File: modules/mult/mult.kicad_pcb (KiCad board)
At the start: 2 copper layers, 18.5 x 111.5 mm, 9 parts, among them J1 Thonkiconn, J2 Thonkiconn, J3 Thonkiconn, J4 Thonkiconn, J5 Thonkiconn, J6 Thonkiconn, J7 Thonkiconn, J8 Thonkiconn

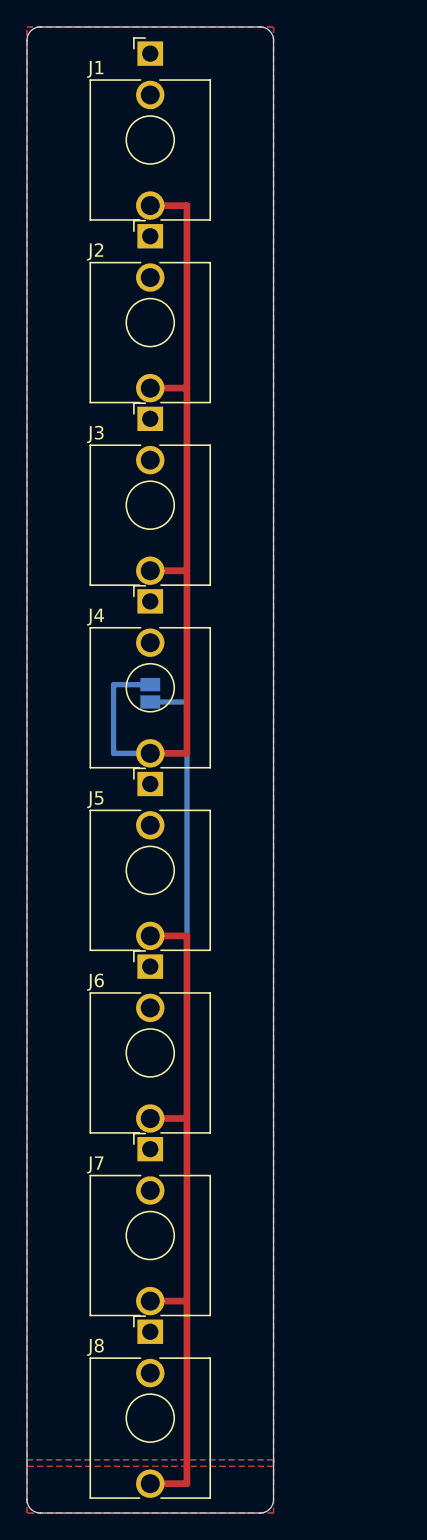
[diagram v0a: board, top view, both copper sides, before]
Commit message: Generate KiCad projects from Haskell: pcbgen toolkit, regenerated mult
toolkit/ is a cabal project that turns a design description
(toolkit/src/Designs/<Name>.hs) into a complete KiCad 10 project: schematic
with embedded library symbols, board with embedded library footprints, project
file with design rules, and custom DRC rules. UUIDs are derived from stable
seeds so regeneration is byte-identical. toolkit/check.sh runs ERC, DRC with
zone refill and schematic parity on a copy in build/, and renders both sides.

modules/mult is now generated. With --severity-all it has zero ERC violations,
zero DRC violations, zero unconnected items and zero parity issues. The
Konnect-made board it replaces had nine library-mismatch warnings and needed
GUI steps to finish.

README.md explains the tool choices (KiCad as compile target, kicad-cli,
KiKit for fab export, Konnect read-only). SETUP.md and CLAUDE.md follow the
new workflow.

Co-Authored-By: Claude Fable 5.1 <noreply@anthropic.com>
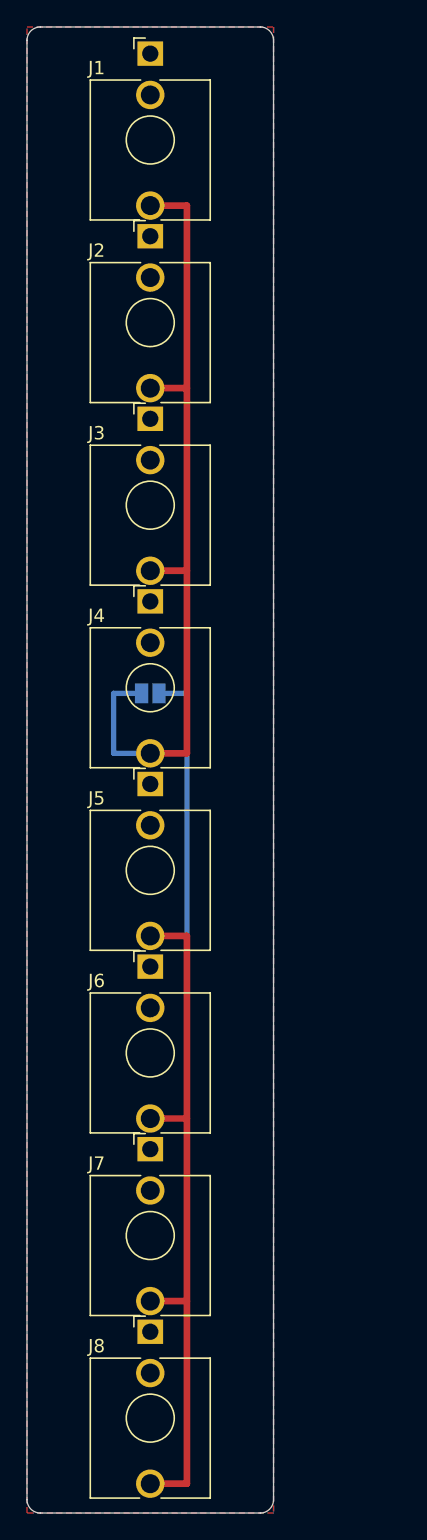
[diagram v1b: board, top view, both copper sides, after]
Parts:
- turned JP1 to 0 degrees
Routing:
- net /MULT_A: track 62.8 -> 61.5 mm
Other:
- board text added: "LINK A-B"
- board text added: "MULT 2x4"

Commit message: Fix Eurorack dimensions: mult becomes 6HP 2x6, add panel project and KiKit export
Doepfer's construction notes and the rail-clearance consensus (PCB <= 108 mm,
centred) showed the 4HP eight-jack column could not fit: the official
Thonkiconn footprint forces a 13.6 mm pitch, and eight of them plus the
barrel and the last body need 110.7 mm. The module is now 6HP with two
columns of six on a 28 x 108 mm board centred behind a 30 x 128.5 mm panel.

- Design.eurorackPanelWidth uses Doepfer's width table; panel height is a
  named constant.
- Designs.MultPanel generates the front panel as its own KiCad project
  (modules/mult/panel) from the same geometry; rail holes at Doepfer
  positions, 6.4 mm jack holes, legend on F.SilkS.
- pcbgen gains 'all' and per-design output directories; parts can hide
  their reference on silkscreen.
- check.sh takes a module sub-directory; fab.sh runs KiKit 1.8.1 (installed
  in KiCad's Python) with --no-drc because its own DRC pass crashes in the
  KiCad 10 bindings. Gerber extents verified: 28.00 x 108.00 and
  30.00 x 128.50 mm.
- Both projects: ERC clean, DRC clean with parity, zero unconnected.

Co-Authored-By: Claude Fable 5.1 <noreply@anthropic.com>
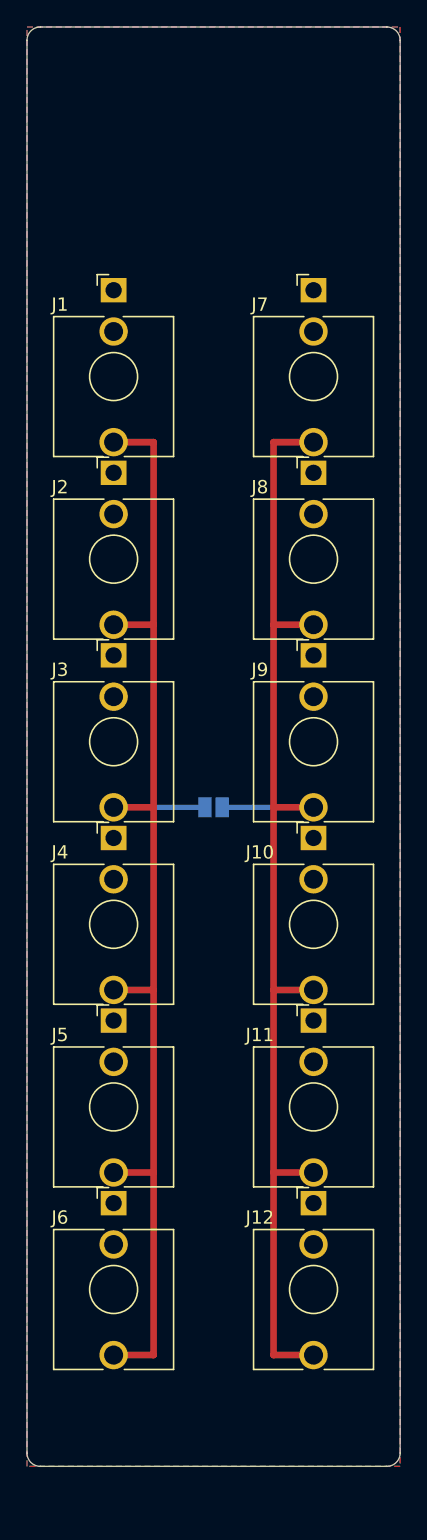
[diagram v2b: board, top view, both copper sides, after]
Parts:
- added J10: Thonkiconn, Connector_Audio:Jack_3.5mm_QingPu_WQP-PJ398SM_Vertical_CircularHoles, F.Cu at (21.5, 60.9)
- added J11: Thonkiconn, Connector_Audio:Jack_3.5mm_QingPu_WQP-PJ398SM_Vertical_CircularHoles, F.Cu at (21.5, 74.5)
- added J12: Thonkiconn, Connector_Audio:Jack_3.5mm_QingPu_WQP-PJ398SM_Vertical_CircularHoles, F.Cu at (21.5, 88.2)
- added J9: Thonkiconn, Connector_Audio:Jack_3.5mm_QingPu_WQP-PJ398SM_Vertical_CircularHoles, F.Cu at (21.5, 47.1)
- moved J7 65.6 mm to (21.5, 19.8)
- moved J8 65.6 mm to (21.5, 33.5)
- moved J2 18.0 mm to (6.50, 33.5)
- moved J1 18.0 mm to (6.50, 19.8)
- moved J3 18.0 mm to (6.50, 47.1)
- moved J4 18.0 mm to (6.50, 60.9)
- moved J5 18.0 mm to (6.50, 74.5)
- moved J6 18.0 mm to (6.50, 88.2)
- moved JP1 9.78 mm to (14.0, 58.5)
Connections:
- J5 pad T: /MULT_B -> /MULT_A
- J6 pad T: /MULT_B -> /MULT_A
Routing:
- net /MULT_A: track 61.5 -> 93.3 mm
- net /MULT_B: track 75.2 -> 93.3 mm
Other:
- board size 18.5 x 111.5 mm -> 28 x 108 mm
- board text added: "A"
- board text added: "B"
- board text added: "MULT 2x6"
- board text removed: "MULT 2x4"

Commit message: Add grid autorouter (A* + negotiated congestion) and route the mult with it
toolkit/src/Route/: pad geometry with exact signed-distance shapes,
footprint pad and keep-out extraction from the emitted board, and a two-layer
grid router. Each net is routed by multi-source A* over cell centres in eight
directions plus via steps; pads of other nets are hard terrain, routed copper
of other nets is a soft cost that grows per iteration (PathFinder-style
negotiated congestion) until no cell is shared. Paths are string-pulled into
any-angle runs with an exact clearance test against pads.

Design gains bdAutoRoute; the mult's hand routing is kept as handRouted but
the board is now produced by the router: one iteration, 0 contested cells,
64 segments, no vias, kicad-cli DRC clean with every severity on.

Co-Authored-By: Claude Fable 5.1 <noreply@anthropic.com>
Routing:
- net /MULT_A: track 93.3 -> 81.1 mm
- net /MULT_B: track 93.3 -> 81.1 mm

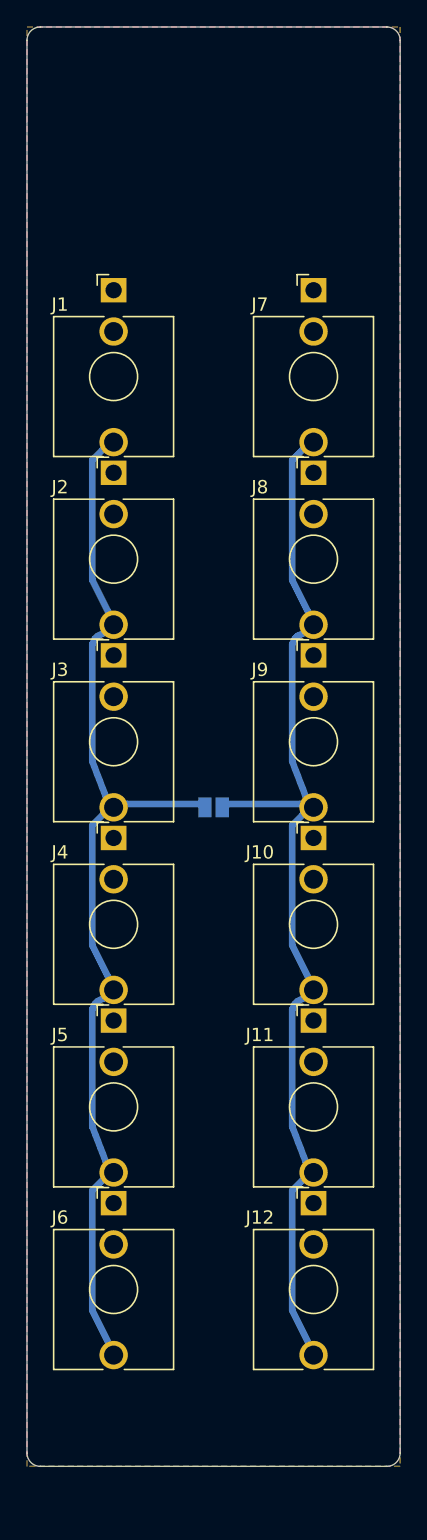
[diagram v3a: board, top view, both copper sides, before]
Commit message: Router: mutable-array A*, reroute only contested nets, octile heuristic, score report
A* now runs in ST over unboxed arrays with a binary heap and a flattened
per-net penalty array instead of immutable Set/IntMap churn (175 GB of
allocation on the stress test). After iteration one only nets that are
in conflict are ripped up; the sharing penalty grows 1.4x per iteration.
Stress test: 86 s -> 3 s CPU, 38 -> 19 iterations, DRC still clean.

pcbgen writes modules/<name>/route-report.md: per-net segments, vias,
length and detour ratio against the Euclidean MST of the pads, so routing
quality is diffable across commits. -O2 and -rtsopts enabled.

Co-Authored-By: Claude Fable 5.1 <noreply@anthropic.com>
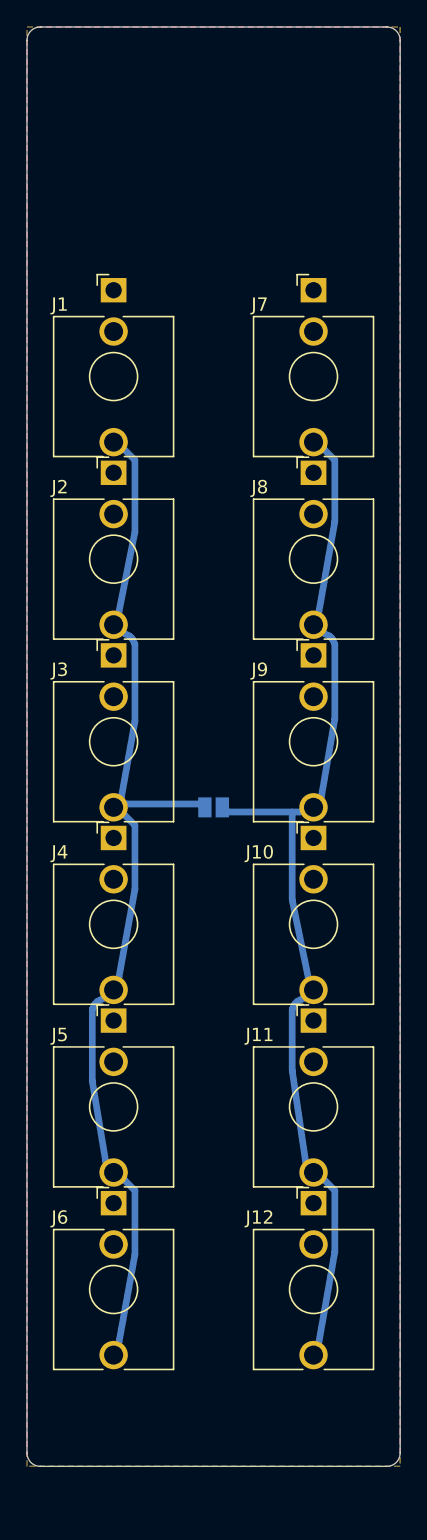
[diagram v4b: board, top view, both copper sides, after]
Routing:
- net /MULT_B: track 81.1 -> 79.3 mm
- net /MULT_A: track 81.1 -> 80.3 mm
